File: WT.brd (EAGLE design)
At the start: 56 x 100 mm, 124 parts, among them IC1 MC7805CDTG, IC2 NE5532D, IC3 NE5532D, IC4 QUAD_OPAMPD, IC5 LM4040B10, IC6 TL072D, Q1 BSS123, Q2 SI2309CDS

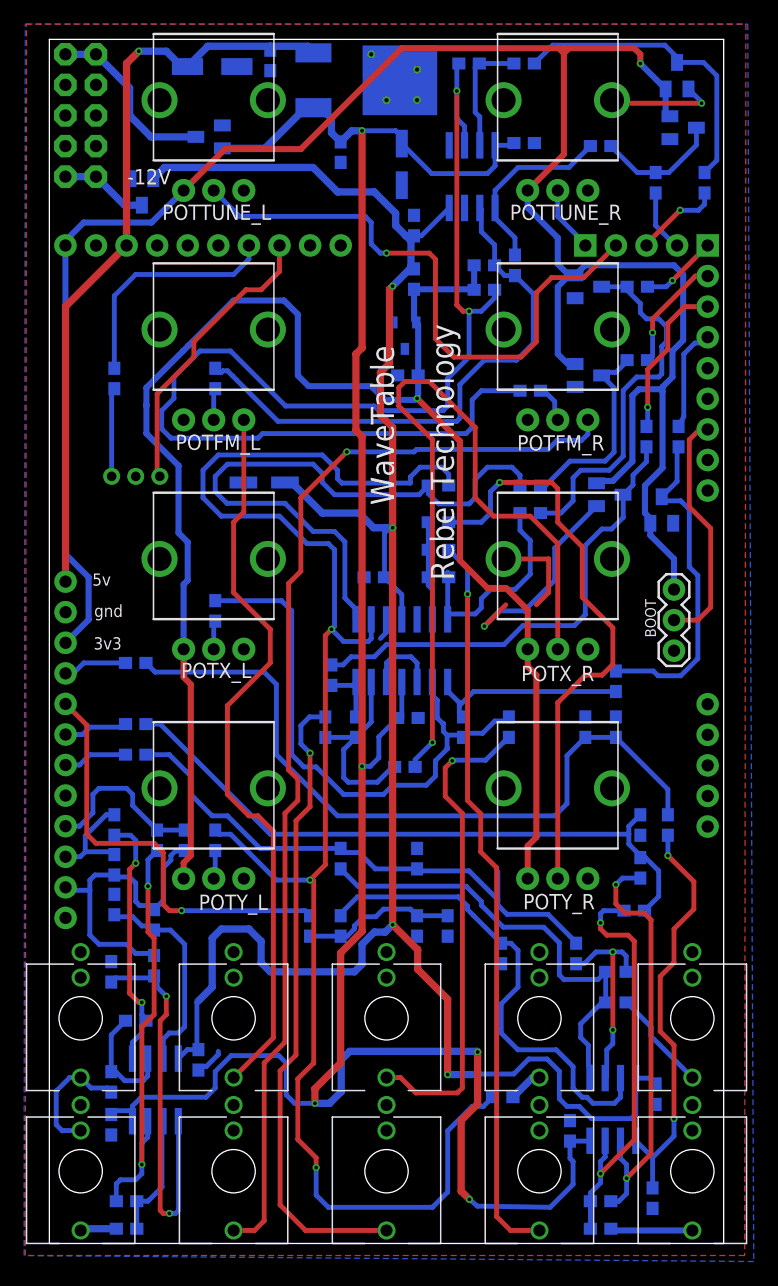
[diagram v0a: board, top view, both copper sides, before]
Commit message: 12 mil clearance update
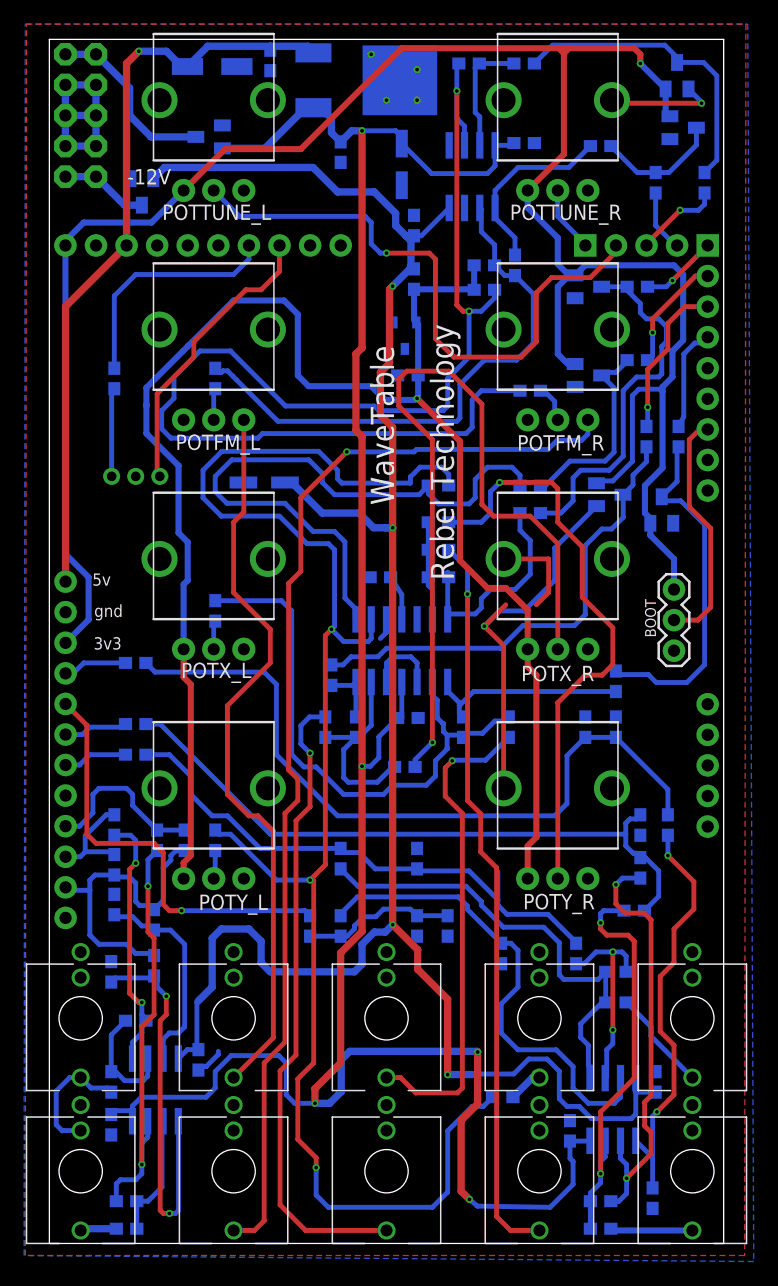
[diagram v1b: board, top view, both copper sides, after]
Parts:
- moved C12 1.02 mm to (50.3, 12.4), turned to 270 degrees
- moved C20 0.51 mm to (27.4, 54.4)
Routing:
- net GND: track 45.1 -> 78.8 mm, vias 2 -> 6
- net N$21: track 64.4 -> 67.0 mm
- net N$16: track 27.7 -> 29.2 mm
- net -12V: track 179.7 -> 178.7 mm
- net N$24: track 54.0 -> 54.6 mm
